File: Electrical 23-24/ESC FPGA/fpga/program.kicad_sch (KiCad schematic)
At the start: 1 part, among them U1 XC6SLX4-TQG144

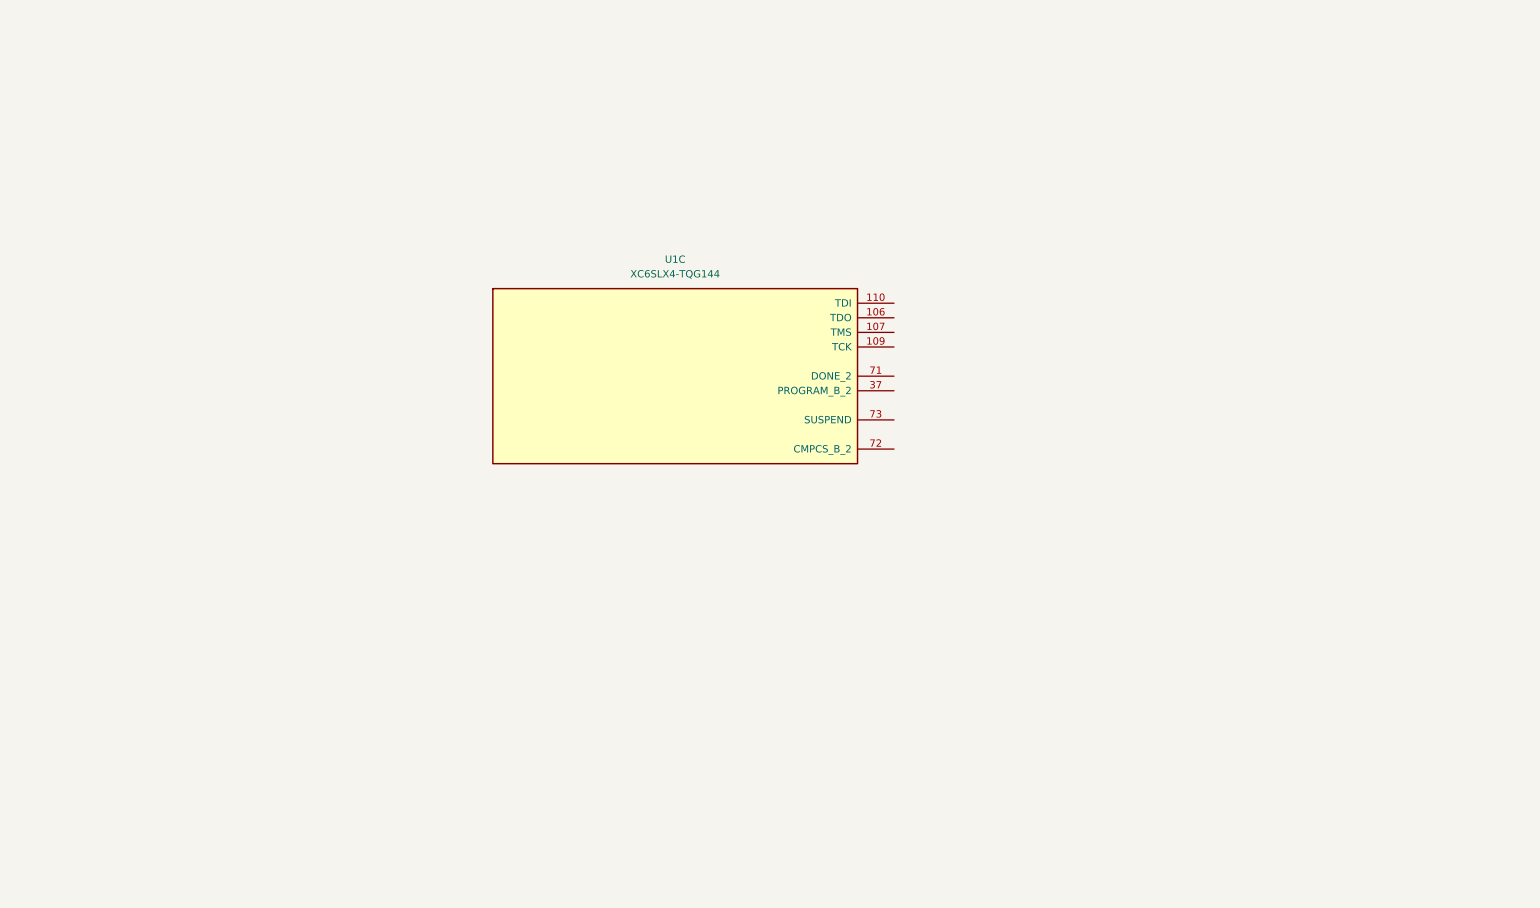
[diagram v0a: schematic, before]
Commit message: Finish programming interface with FPGA
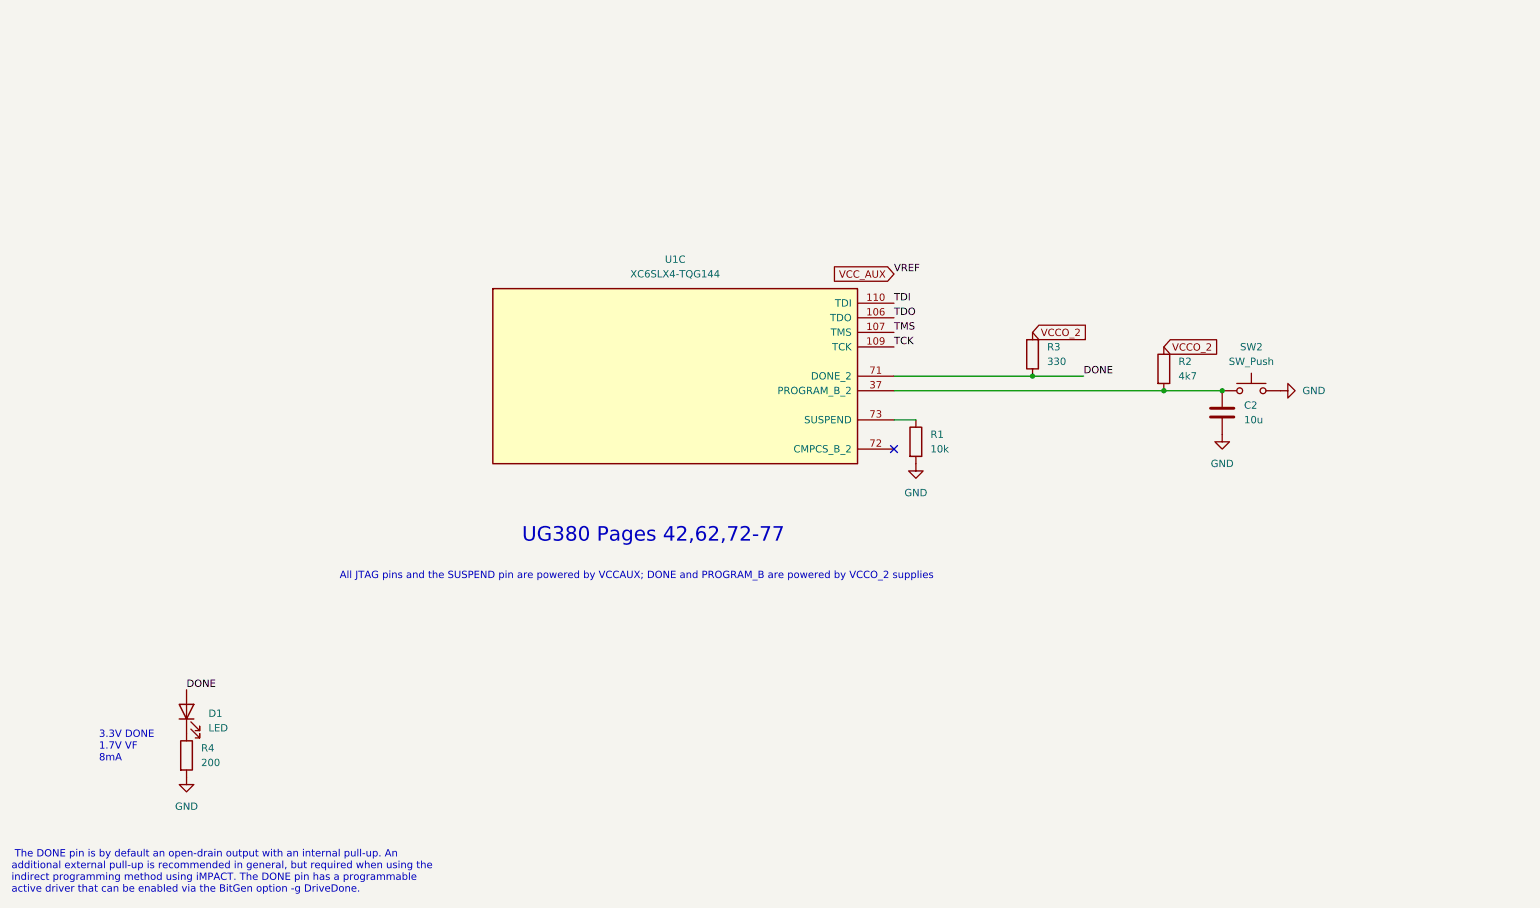
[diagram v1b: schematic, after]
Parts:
- added C2: 10u, symbol Device:C
- added D1: LED, symbol Device:LED
- added R1: 10k, symbol Device:R
- added R2: 4k7, symbol Device:R
- added R3: 330, symbol Device:R
- added R4: 200, symbol Device:R
- added SW2: SW_Push, symbol Switch:SW_Push
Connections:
- net TDO: now reaches U1.106 (TDO)
- net TMS: now reaches U1.107 (TMS)
- net TCK: now reaches U1.109 (TCK)
- net TDI: now reaches U1.110 (TDI)
- net at U1.37 (PROGRAM_B_2): now also C2.1, R2.2, SW2.1
- net DONE: now reaches U1.71 (DONE_2)
- net DONE: now also D1.2 (A), R3.1
- net at U1.73 (SUSPEND): now also R1.1
- new net: D1.1 (K), R4.1
- new net GND: C2.2, R1.2, R4.2, SW2.2
- new net VCCO_2: R2.1, R3.2
- no-connect marks 0 -> 1
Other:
- note added: "3.3V DONE 1.7V VF 8mA"
- note added: "All JTAG pins and the SUSPEND pin are powered by VCCAUX; DONE and PROGRAM_B are powered by VCCO_2 supplies"
- note added: "The DONE pin is by default an open-drain output with an internal pull-up. An additional external pull-up is recommended in general, but required when using the indirect programming method using iMPACT. The DONE pin has a programmable active driver that can be enabled via the BitGen option -g DriveDone."
- note added: "UG380 Pages 42,62,72-77"

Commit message: Add programmer
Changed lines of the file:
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@@
     (effects (font (size 2.54 2.54)) (justify left bottom))
   )
-  (label "TCK" (at 179.07 85.09 0) (fields_autoplaced)
-    (effects (font (size 1.27 1.27)) (justify left bottom))
-  )
-  (label "TDO" (at 179.07 80.01 0) (fields_autoplaced)
-    (effects (font (size 1.27 1.27)) (justify left bottom))
-  )
   (label "DONE" (at 212.09 90.17 0) (fields_autoplaced)
-    (effects (font (size 1.27 1.27)) (justify left bottom))
-  )
-  (label "TMS" (at 179.07 82.55 0) (fields_autoplaced)
-    (effects (font (size 1.27 1.27)) (justify left bottom))
-  )
-  (label "TDI" (at 179.07 77.47 0) (fields_autoplaced)
-    (effects (font (size 1.27 1.27)) (justify left bottom))
-  )
-  (label "VREF" (at 179.07 72.39 0) (fields_autoplaced)
     (effects (font (size 1.27 1.27)) (justify left bottom))
   )
@@
     )
   )
+  (global_label "TCK" (shape input) (at 179.07 85.09 0) (fields_autoplaced)
+    (effects (font (size 1.27 1.27)) (justify left))
+    (property "Intersheetrefs" "${INTERSHEET_REFS}" (at 185.5628 85.09 0)
+      (effects (font (size 1.27 1.27)) (justify left) hide)
+    )
+  )
+  (global_label "TMS" (shape input) (at 179.07 82.55 0) (fields_autoplaced)
+    (effects (font (size 1.27 1.27)) (justify left))
+    (property "Intersheetrefs" "${INTERSHEET_REFS}" (at 185.6837 82.55 0)
+      (effects (font (size 1.27 1.27)) (justify left) hide)
+    )
+  )
+  (global_label "TDI" (shape input) (at 179.07 77.47 0) (fields_autoplaced)
+    (effects (font (size 1.27 1.27)) (justify left))
+    (property "Intersheetrefs" "${INTERSHEET_REFS}" (at 184.8976 77.47 0)
+      (effects (font (size 1.27 1.27)) (justify left) hide)
+    )
+  )
+  (global_label "VREF" (shape input) (at 179.07 72.39 0) (fields_autoplaced)
+    (effects (font (size 1.27 1.27)) (justify left))
+    (property "Intersheetrefs" "${INTERSHEET_REFS}" (at 186.6514 72.39 0)
+      (effects (font (size 1.27 1.27)) (justify left) hide)
+    )
+  )
   (global_label "VCC_AUX" (shape input) (at 179.07 72.39 180) (fields_autoplaced)
     (effects (font (size 1.27 1.27)) (justify right))
@@
     )
   )
+  (global_label "TDO" (shape input) (at 179.07 80.01 0) (fields_autoplaced)
+    (effects (font (size 1.27 1.27)) (justify left))
+    (property "Intersheetrefs" "${INTERSHEET_REFS}" (at 185.6233 80.01 0)
+      (effects (font (size 1.27 1.27)) (justify left) hide)
+    )
+  )

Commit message: idk but something
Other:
- note added: "does fpga power vref or not? seems like both external power and internal..."
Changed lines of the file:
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@@
+    (effects (font (size 1.27 1.27)) (justify left bottom))
+  )
+  (text "does fpga power vref or not?\nseems like both external power and internal..."
+    (at 166.37 67.31 0)
     (effects (font (size 1.27 1.27)) (justify left bottom))
   )

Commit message: DR Feedback
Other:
- note added: "mosfet?"
- note added: "test point"
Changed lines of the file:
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@@
+    (effects (font (size 1.27 1.27)) (justify left bottom))
+  )
+  (text "test point" (at 220.98 99.06 0)
     (effects (font (size 1.27 1.27)) (justify left bottom))
   )
@@
     (effects (font (size 2.54 2.54)) (justify left bottom))
   )
+  (text "mosfet?" (at 73.66 153.67 0)
+    (effects (font (size 1.27 1.27)) (justify left bottom))
+  )
   (label "DONE" (at 212.09 90.17 0) (fields_autoplaced)

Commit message: Add fpga stuff and stencils
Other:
- note added: "DONE is open drain until boot-up"
- note added: "PROGRAM_B LOW triggers reconfiguration"
- note added: "SUSPEND must be connected to ground if not used"
- note added: "does fpga power vref or not? seems like both external power and internal... UPDATE SEEMS LIKE IT DOES"
- note removed: "does fpga power vref or not? seems like both external power and internal..."
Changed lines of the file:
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@@
     (effects (font (size 1.27 1.27)) (justify left bottom))
   )
-  (text "does fpga power vref or not?\nseems like both external power and internal..."
+  (text "DONE is open drain until boot-up" (at 201.93 80.01 0)
+    (effects (font (size 1.27 1.27)) (justify left bottom))
+  )
+  (text "PROGRAM_B LOW triggers reconfiguration" (at 241.3 105.41 0)
+    (effects (font (size 1.27 1.27)) (justify left bottom))
+  )
+  (text "does fpga power vref or not?\nseems like both external power and internal...\nUPDATE SEEMS LIKE IT DOES"
     (at 166.37 67.31 0)
     (effects (font (size 1.27 1.27)) (justify left bottom))
@@
   (text "UG380 Pages 42,62,72-77" (at 114.3 119.38 0)
     (effects (font (size 2.54 2.54)) (justify left bottom))
+  )
+  (text "SUSPEND must be connected to ground if not used" (at 181.61 114.3 0)
+    (effects (font (size 1.27 1.27)) (justify left bottom))
   )
   (text "mosfet?" (at 73.66 153.67 0)
@@
     )
   )
+  (global_label "GND" (shape input) (at 266.7 34.29 90) (fields_autoplaced)
+    (effects (font (size 1.27 1.27)) (justify left))
+    (property "Intersheetrefs" "${INTERSHEET_REFS}" (at 266.7 27.4343 90)
+      (effects (font (size 1.27 1.27)) (justify left) hide)
+    )
+  )
   (global_label "TDO" (shape input) (at 179.07 80.01 0) (fields_autoplaced)
     (effects (font (size 1.27 1.27)) (justify left))
@@
         )
       )
+    )
+  )
+  (symbol (lib_id "power:GND") (at 266.7 34.29 0) (unit 1)
+    (in_bom yes) (on_board yes) (dnp no) (fields_autoplaced)
+    (property "Reference" "#PWR016" (at 266.7 40.64 0)
+      (effects (font (size 1.27 1.27)) hide)
+    )
+    (property "Value" "GND" (at 266.7 39.37 0)
+      (effects (font (size 1.27 1.27)))
+    )
+    (property "Footprint" "" (at 266.7 34.29 0)
+      (effects (font (size 1.27 1.27)) hide)
+    )
+    (property "Datasheet" "" (at 266.7 34.29 0)
+      (effects (font (size 1.27 1.27)) hide)
+    )
+    (pin "1")
+    (instances
+      (project "fpga"
+        (path "/5bf59577-a814-4364-8f7a-37815cfb5474/3e04db34-3f8a-4742-be82-6fa24c009343"
+          (reference "#PWR016") (unit 1)
+        )
+        (path "/5bf59577-a814-4364-8f7a-37815cfb5474/1f83b38b-56ef-4110-879b-13379f9dd920"
+          (reference "#PWR026") (unit 1)
+        )
+        (path "/5bf59577-a814-4364-8f7a-37815cfb5474/a286b274-4434-47ab-983d-e64806fdcbd6"
+          (reference "#PWR036") (unit 1)
+        )
+        (path "/5bf59577-a814-4364-8f7a-37815cfb5474/5e885406-1c13-459a-ba1f-8e2447b7cb89"
+          (reference "#PWR039") (unit 1)
+        )
+      )

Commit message: Working on FPGA board
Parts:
- removed R1: 10k, symbol Device:R
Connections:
- net GND: now also U1.73 (SUSPEND)
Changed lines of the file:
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@@
     (effects (font (size 2.54 2.54)) (justify left bottom))
   )
-  (text "SUSPEND must be connected to ground if not used" (at 181.61 114.3 0)
+  (text "SUSPEND must be connected to ground if not used" (at 181.61 106.68 0)
     (effects (font (size 1.27 1.27)) (justify left bottom))
   )
@@
     )
   )
-  (symbol (lib_id "power:GND") (at 182.88 105.41 0) (unit 1)
-    (in_bom yes) (on_board yes) (dnp no) (fields_autoplaced)
-    (property "Reference" "#PWR01" (at 182.88 111.76 0)
-      (effects (font (size 1.27 1.27)) hide)
-    )
-    (property "Value" "GND" (at 182.88 110.49 0)
-      (effects (font (size 1.27 1.27)))
-    )
-    (property "Footprint" "" (at 182.88 105.41 0)
-      (effects (font (size 1.27 1.27)) hide)
-    )
-    (property "Datasheet" "" (at 182.88 105.41 0)
+  (symbol (lib_id "power:GND") (at 182.88 97.79 0) (unit 1)
+    (in_bom yes) (on_board yes) (dnp no) (fields_autoplaced)
+    (property "Reference" "#PWR01" (at 182.88 104.14 0)
+      (effects (font (size 1.27 1.27)) hide)
+    )
+    (property "Value" "GND" (at 182.88 102.87 0)
+      (effects (font (size 1.27 1.27)))
+    )
+    (property "Footprint" "" (at 182.88 97.79 0)
+      (effects (font (size 1.27 1.27)) hide)
+    )
+    (property "Datasheet" "" (at 182.88 97.79 0)
       (effects (font (size 1.27 1.27)) hide)
     )
@@
         )
       )
-    )
-  )
-  (symbol (lib_id "Device:R") (at 182.88 101.6 0) (unit 1)
-    (in_bom yes) (on_board yes) (dnp no) (fields_autoplaced)
-    (property "Reference" "R1" (at 185.42 100.33 0)
-      (effects (font (size 1.27 1.27)) (justify left))
-    )
-    (property "Value" "10k" (at 185.42 102.87 0)
-      (effects (font (size 1.27 1.27)) (justify left))
-    )
-    (property "Footprint" "" (at 181.102 101.6 90)
-      (effects (font (size 1.27 1.27)) hide)
-    )
-    (property "Datasheet" "~" (at 182.88 101.6 0)
-      (effects (font (size 1.27 1.27)) hide)
-    )
-    (pin "1")
-    (pin "2")
-    (instances
-      (project "fpga"
-        (path "/5bf59577-a814-4364-8f7a-37815cfb5474/5e885406-1c13-459a-ba1f-8e2447b7cb89"
-          (reference "R1") (unit 1)
-        )
-      )
